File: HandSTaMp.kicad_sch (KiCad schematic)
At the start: 25 parts, among them J1 USB_C_Receptacle_USB2.0_16P, J2 Pins, J3 SWD, J4 C15, SW0 BOOT, SW1 Row 0, Col 0, SW2 Row 0, Col 1, U1 STM32C071GBUx, U2 PRTR5V0U2X, U3 XC6206P332MR-G

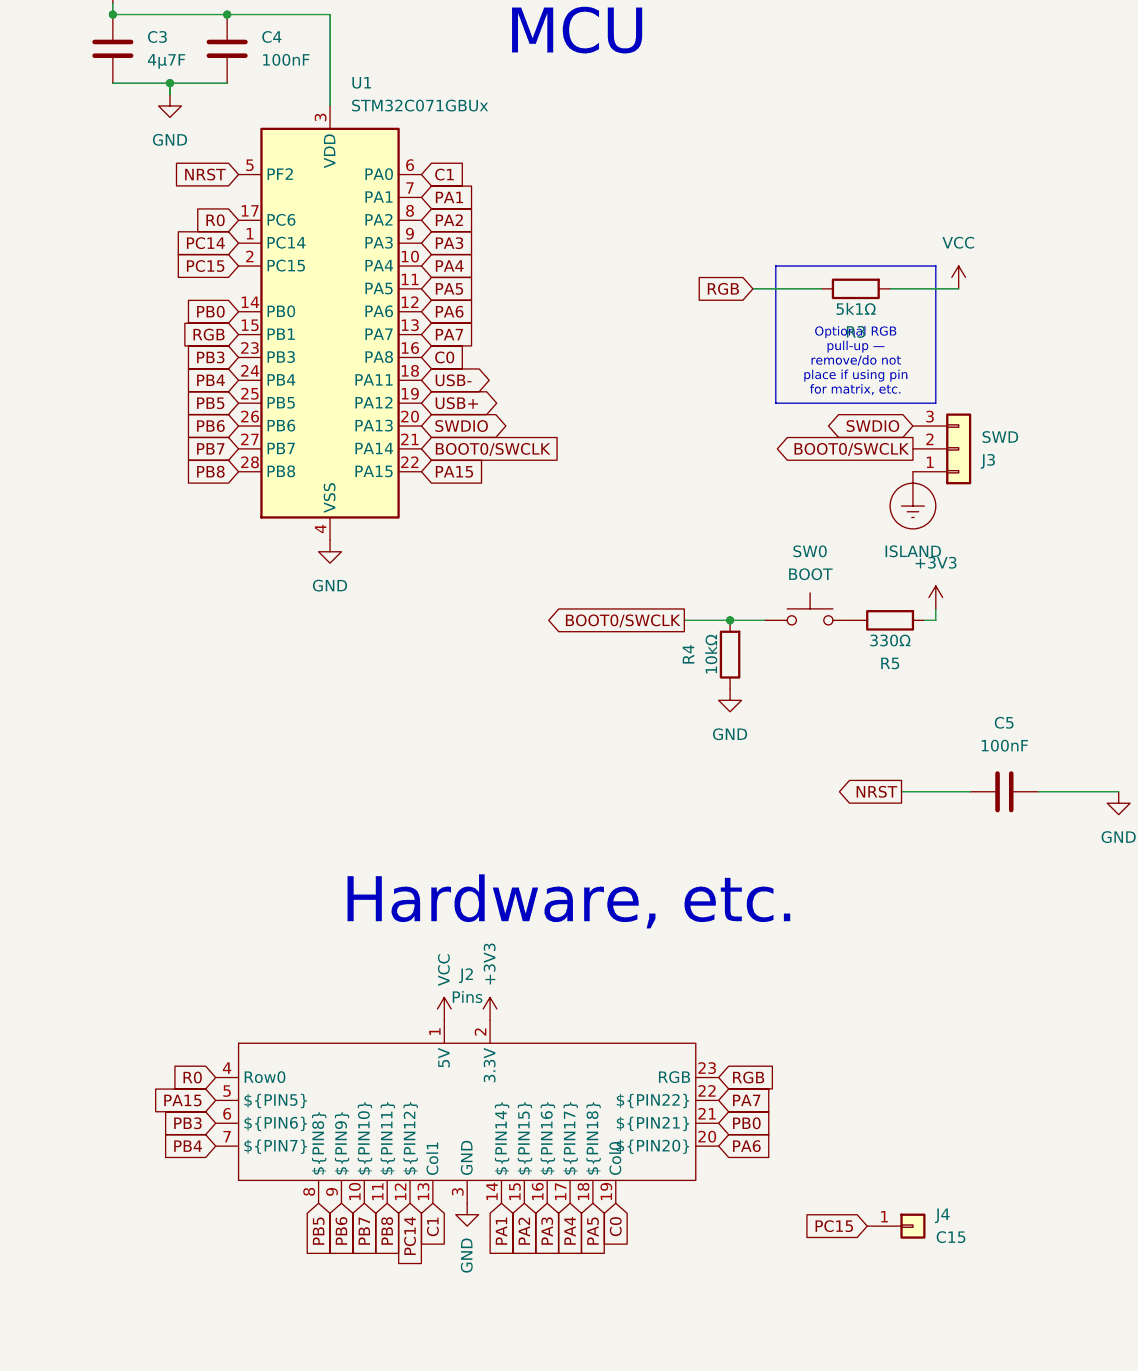
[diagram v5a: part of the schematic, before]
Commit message: Move pad GPIO to THT connection
 * PC15 pad removed
 * Col1 switched to PC15
 * GND pin near right corner switched to GPIO
 * Bottom right pin assignments shuffled over one
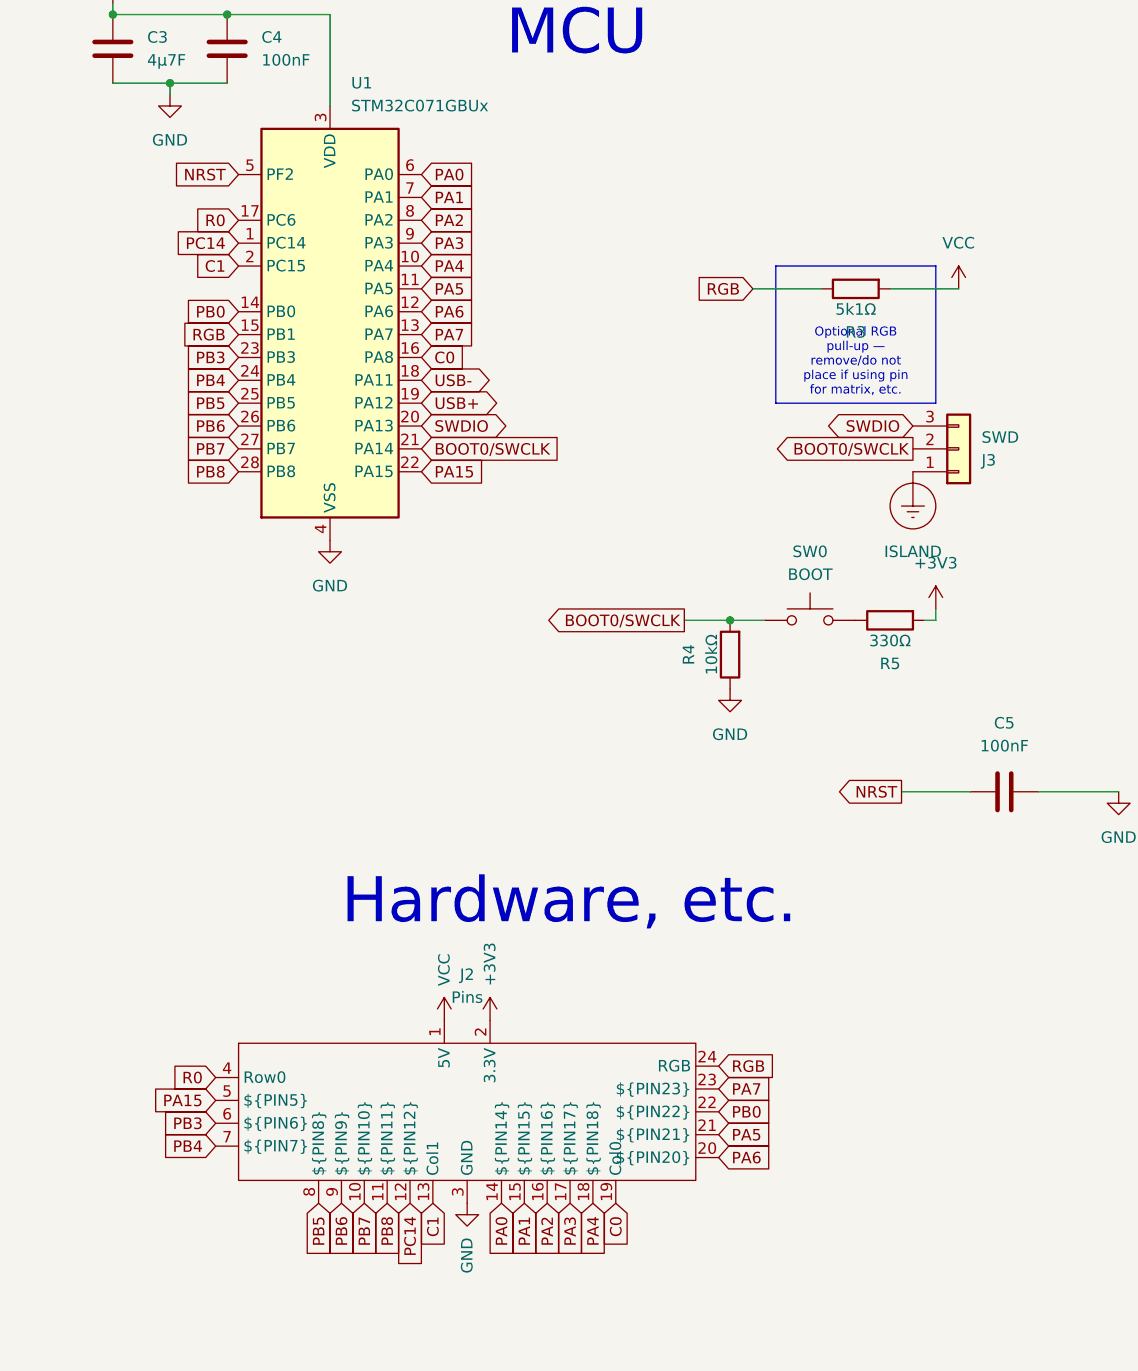
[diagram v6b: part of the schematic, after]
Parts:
- removed J4: C15, Project Library:TestPoint_Pad_1.5x1.5mm, symbol Connector_Generic:Conn_01x01
- J2: PIN14 A1 -> A0; PIN15 A2 -> A1; PIN16 A3 -> A2; PIN17 A4 -> A3; PIN18 A5 -> A4; PIN21 B0 -> A5; PIN22 A7 -> B0; PIN23 (none) -> A7
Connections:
- net PC15 is gone; now on net C1: U1.2 (PC15)
- net C1: no longer U1.6 (PA0)
- net PA1: now also J2.15 (${PIN15}); no longer J2.14 (${PIN14})
- net PA2: now also J2.16 (${PIN16}); no longer J2.15 (${PIN15})
- net PA3: now also J2.17 (${PIN17}); no longer J2.16 (${PIN16})
- net PA4: now also J2.18 (${PIN18}); no longer J2.17 (${PIN17})
- net PA5: now also J2.21 (${PIN21}); no longer J2.18 (${PIN18})
- net PA7: now also J2.23 (${PIN23}); no longer J2.22 (${PIN22})
- net PB0: now also J2.22 (${PIN22}); no longer J2.21 (${PIN21})
- net RGB: now also J2.24 (RGB); no longer J2.23 (RGB)
- new net PA0: J2.14 (${PIN14}), U1.6 (PA0)

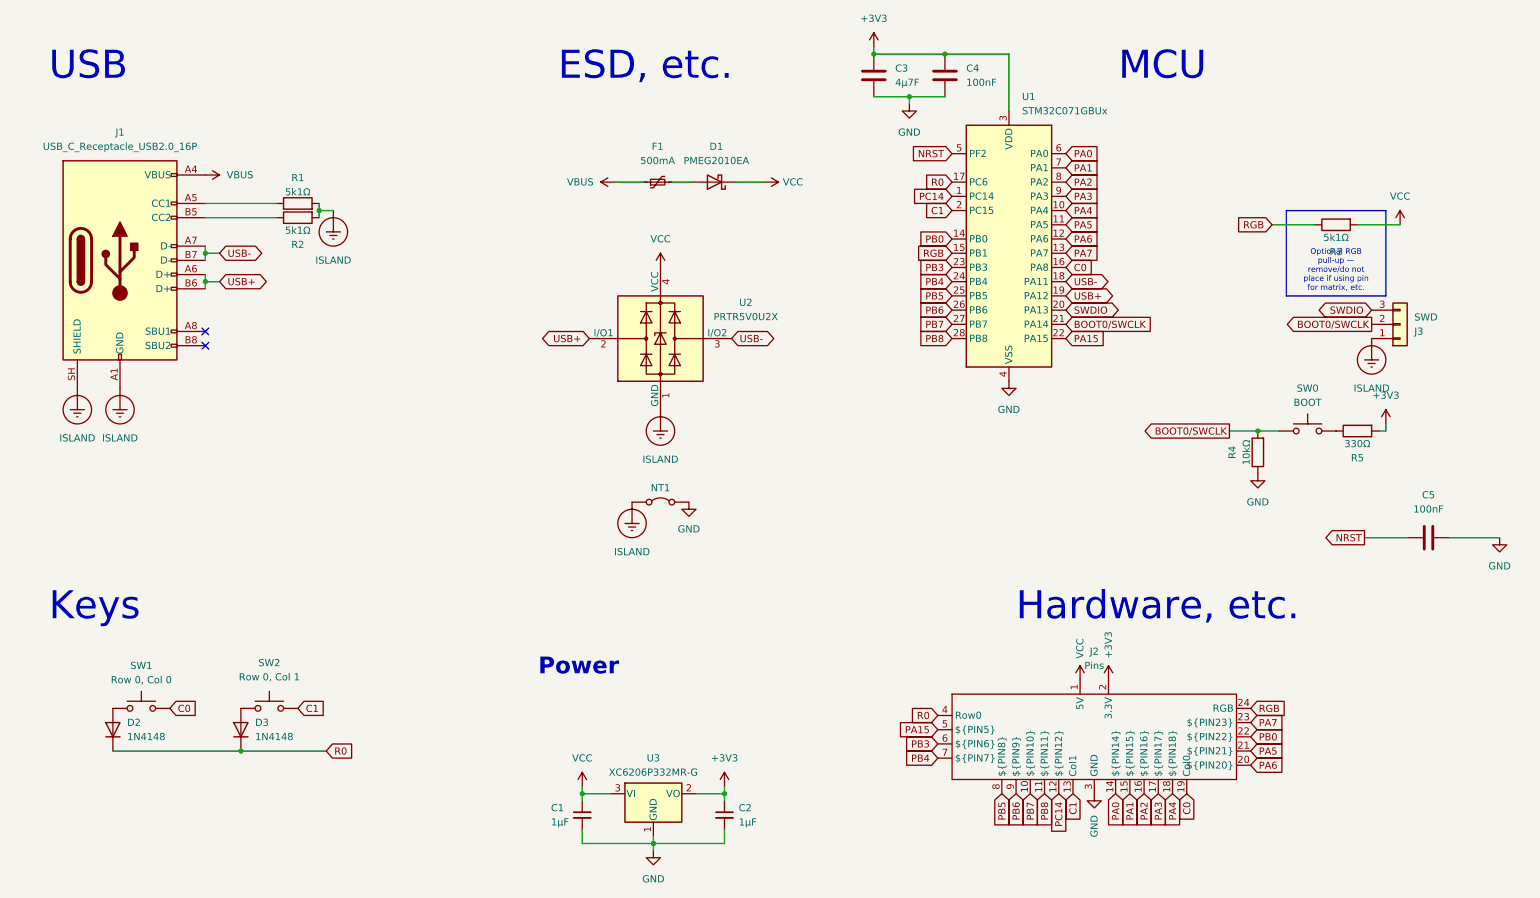
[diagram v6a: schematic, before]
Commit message: Update schematic presentation, check ERC and DRC
Also, fix slight misalignment of external pins on PCB.
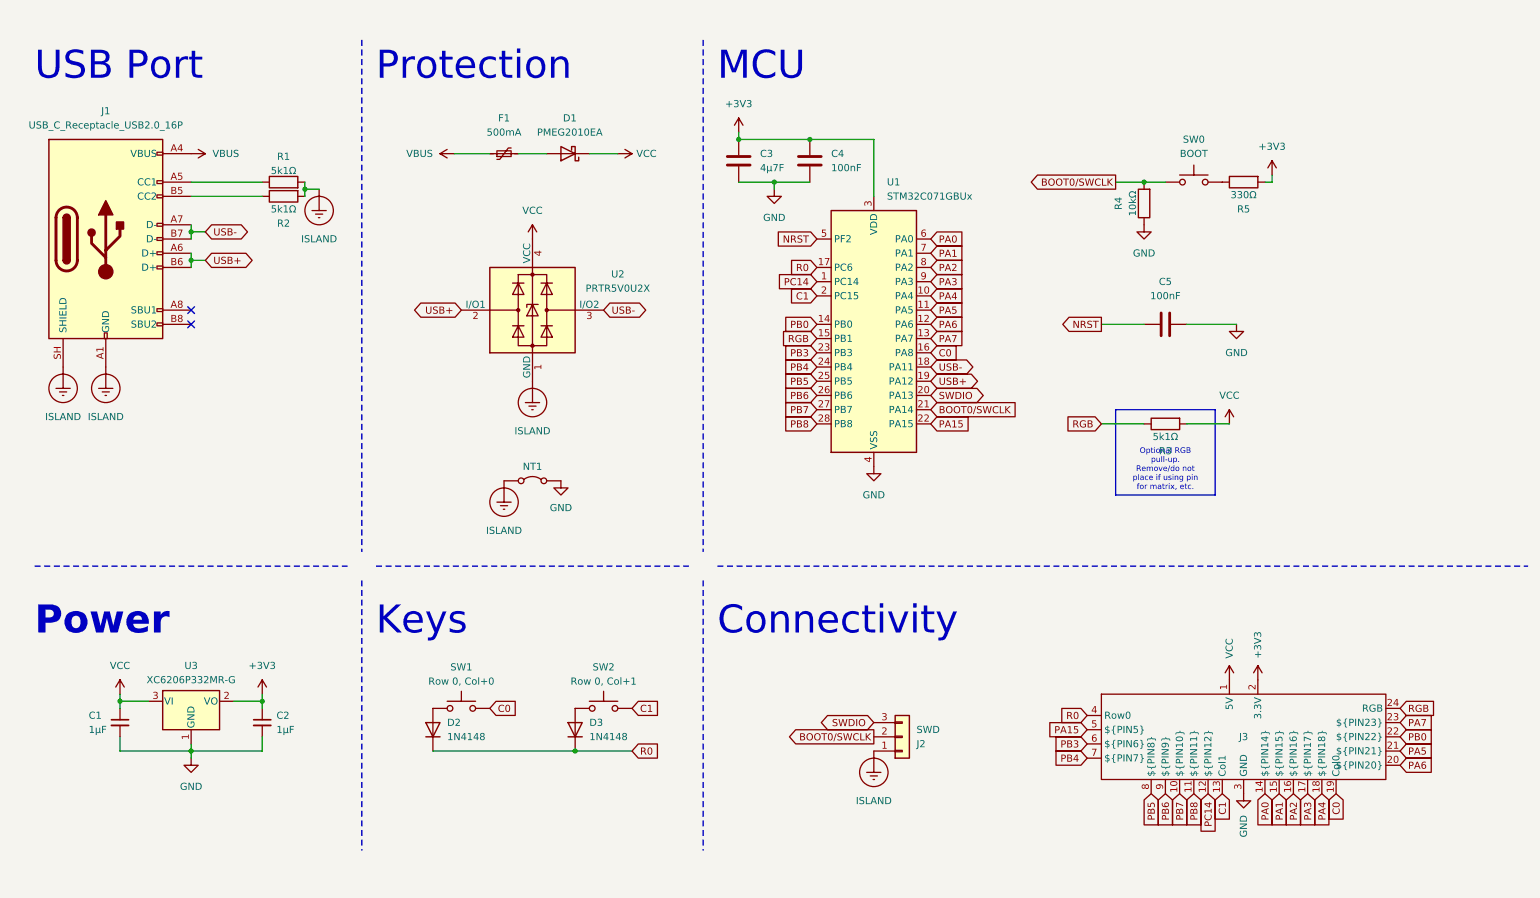
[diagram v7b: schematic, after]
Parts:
- SW1: value Row 0, Col 0 -> Row 0, Col+0
- SW2: value Row 0, Col 1 -> Row 0, Col+1
- renumbered J3 to J2, J2 to J3
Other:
- note added: "Connectivity"
- note added: "Protection"
- note added: "USB Port"
- note removed: "ESD, etc."
- note removed: "Hardware, etc."
- note removed: "USB"
- moved on the sheet: C1, C2, C3, C4, C5, D1, D2, D3, F1, J1, J2, J3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
